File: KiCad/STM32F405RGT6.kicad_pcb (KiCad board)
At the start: 4 copper layers, 101.6 x 101.6 mm, 61 parts, among them J1 Conn_02x05_Odd_Even, J2 USB_C_Receptacle_USB2.0, J3 Conn_02x32_Odd_Even, J4 Conn_02x20_Odd_Even, SW1 TS-1187A, SW2 TS-1187A, U1 M24C02-RMN, U2 STM32F405RGTx, U3 AMS1117-3.3, U4 SRV05-4, Y1 16MHz

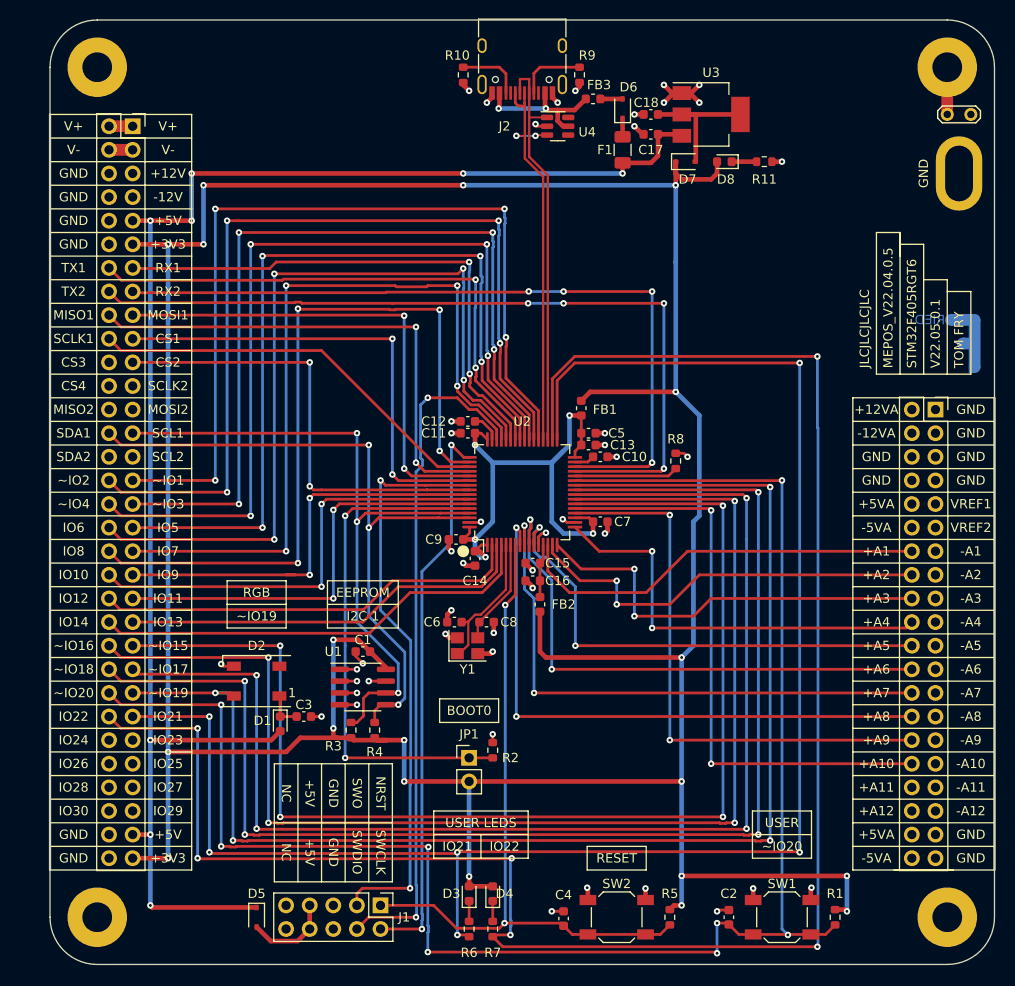
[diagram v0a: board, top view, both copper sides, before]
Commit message: Fixed some DRC errors
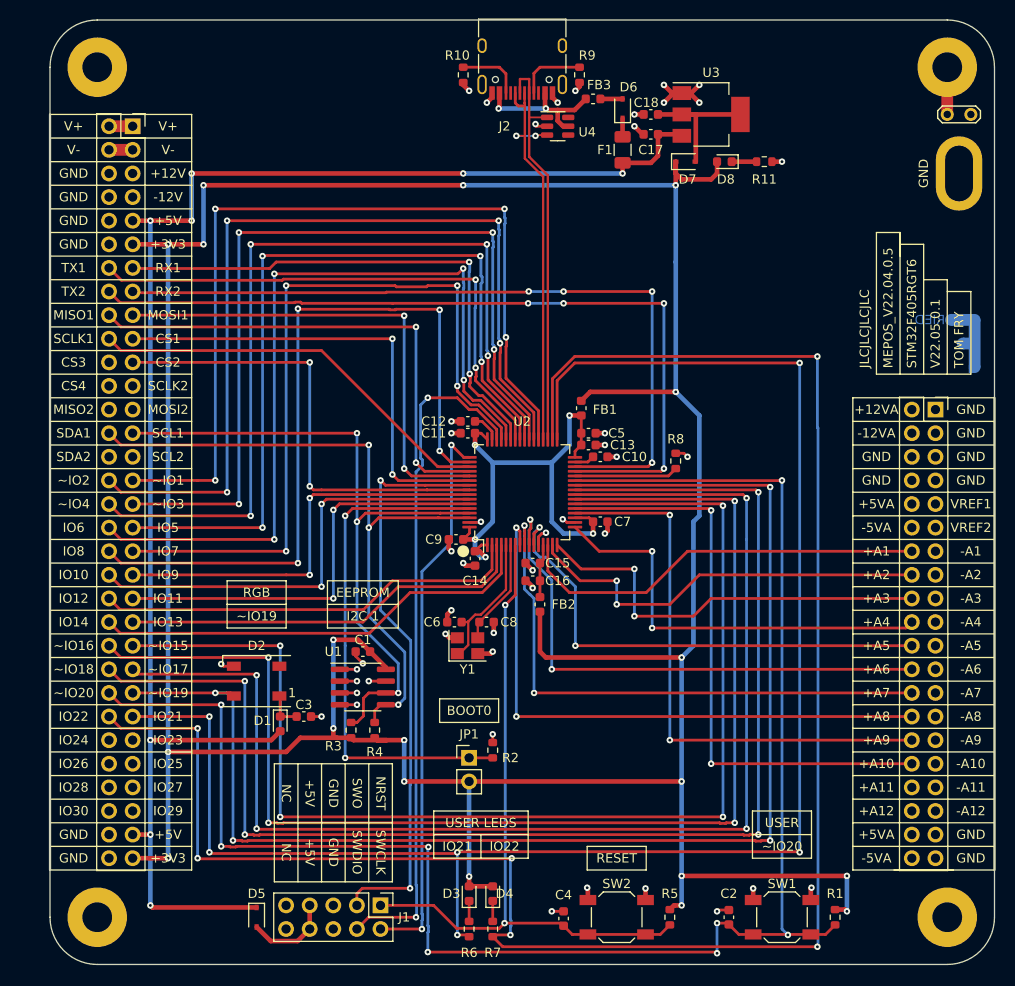
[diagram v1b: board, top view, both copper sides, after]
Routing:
- net /VDD_Decoupling: track 57.9 -> 56.1 mm
- net GPIO9: track 45.6 -> 44.6 mm
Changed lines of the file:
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@@
   (segment (start 89.526882 95.068119) (end 89.523186 95.068119) (width 0.5) (layer "F.Cu") (net 1))
   (segment (start 68.785 105.08) (end 70.625 105.08) (width 0.3) (layer "F.Cu") (net 1))
-  (segment (start 113.17 127.305) (end 113.245 127.38) (width 0.3) (layer "F.Cu") (net 1))
   (segment (start 91.655 41.815) (end 91.655 42.29) (width 0.5) (layer "F.Cu") (net 1))
   (segment (start 90.945 89.135555) (end 90.958029 89.122526) (width 0.3) (layer "F.Cu") (net 1))
@@
   (segment (start 105.575 41.82) (end 106.58 41.82) (width 0.5) (layer "F.Cu") (net 1))
   (segment (start 90.155 90.435) (end 90.155 89.559639) (width 0.3) (layer "F.Cu") (net 1))
-  (segment (start 101.74 127.305) (end 101.665 127.38) (width 0.3) (layer "F.Cu") (net 1))
   (segment (start 85.015 102.12) (end 85.23 101.905) (width 0.5) (layer "F.Cu") (net 1))
   (segment (start 113.245 128.63) (end 113.245 127.38) (width 0.5) (layer "F.Cu") (net 1))
@@
   (segment (start 63.005 93.65) (end 46.495 93.65) (width 0.3) (layer "F.Cu") (net 25))
   (segment (start 65.93 85.01) (end 82.73 85.01) (width 0.3) (layer "F.Cu") (net 25))
-  (segment (start 63.994259 93.65) (end 63.005 93.65) (width 0.3) (layer "F.Cu") (net 25))
   (segment (start 65.545 85.395) (end 65.93 85.01) (width 0.3) (layer "F.Cu") (net 25))
   (via (at 65.545 93.65) (size 0.7) (drill 0.3) (layers "F.Cu" "B.Cu") (net 25))
@@
   (segment (start 83.953802 97.93048) (end 86.655 95.229282) (width 0.25) (layer "F.Cu") (net 91))
   (segment locked (start 134.125 44.12) (end 134.125 39.04) (width 1.27) (layer "F.Cu") (net 92))
-  (segment locked (start 134.379 39.294) (end 134.125 39.04) (width 1.27) (layer "F.Cu") (net 92))
   (segment (start 82.69 113.335) (end 85.23 113.335) (width 0.3) (layer "F.Cu") (net 95))
   (segment (start 81.028564 86.50952) (end 81.029044 86.51) (width 0.3) (layer "F.Cu") (net 95))
@@
   (segment (start 89.19 44.44) (end 89.155 44.405) (width 0.2) (layer "F.Cu") (net 104))
   (segment (start 91.155 50.68) (end 91.155 79.085) (width 0.254) (layer "F.Cu") (net 104))
-  (segment (start 89.154511 41.814511) (end 89.155 41.815) (width 0.3) (layer "F.Cu") (net 104))
   (segment (start 89.155 41.815) (end 89.155 48.68) (width 0.254) (layer "F.Cu") (net 104))
   (segment (start 89.155 48.68) (end 91.155 50.68) (width 0.254) (layer "F.Cu") (net 104))
@@
   (segment (start 85.23 81.585) (end 91.58 81.585) (width 0.5) (layer "B.Cu") (net 105))
   (segment (start 84.4555 91.745) (end 83.96 91.745) (width 0.5) (layer "B.Cu") (net 105))
-  (segment (start 91.58 81.585) (end 92.85 80.315) (width 0.5) (layer "B.Cu") (net 105))
   (segment (start 85.23 87.935) (end 85.23 81.585) (width 0.5) (layer "B.Cu") (net 105))
   (segment (start 91.58 87.935) (end 91.58 81.585) (width 0.5) (layer "B.Cu") (net 105))

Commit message: Updated PCB
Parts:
- moved U4 3.30 mm to (88.9, 45.4)
- moved JP1 1.27 mm to (82.7, 112.1)
- moved R2 1.08 mm to (85.2, 111.4)
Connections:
- U4 pad 1: /STM32_USBD- -> /STM32_USBD+
- U4 pad 3: /STM32_USBD+ -> unconnected-(U4-Pad3)
- U4 pad 6: unconnected-(U4-Pad6) -> /STM32_USBD-
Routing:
- net GPIO7: track 82.6 -> 63.3 mm, vias 4 -> 2
- net GPIO8: track 82.4 -> 66.1 mm
- net GPIO15~: track 131.4 -> 123.4 mm
- net GPIO16~: track 137.6 -> 130.9 mm
- net GPIO17~: track 137.0 -> 131.8 mm
- net GND: track 64.5 -> 69.6 mm, vias 45 -> 47
- net GPIO21: track 182.6 -> 177.6 mm
- net SCLK1: track 44.5 -> 48.9 mm, vias 0 -> 2
- net GPIO20~: track 181.1 -> 176.6 mm
- net GPIO18~: track 143.7 -> 139.7 mm
- net GPIO19~: track 145.4 -> 141.8 mm
- net GPIO22: track 203.2 -> 199.7 mm
- net /STM32_USBD+: track 44.6 -> 41.2 mm, vias 2 -> 0
- net SWDIO: track 73.4 -> 70.3 mm
- net CS2: track 49.7 -> 46.8 mm
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
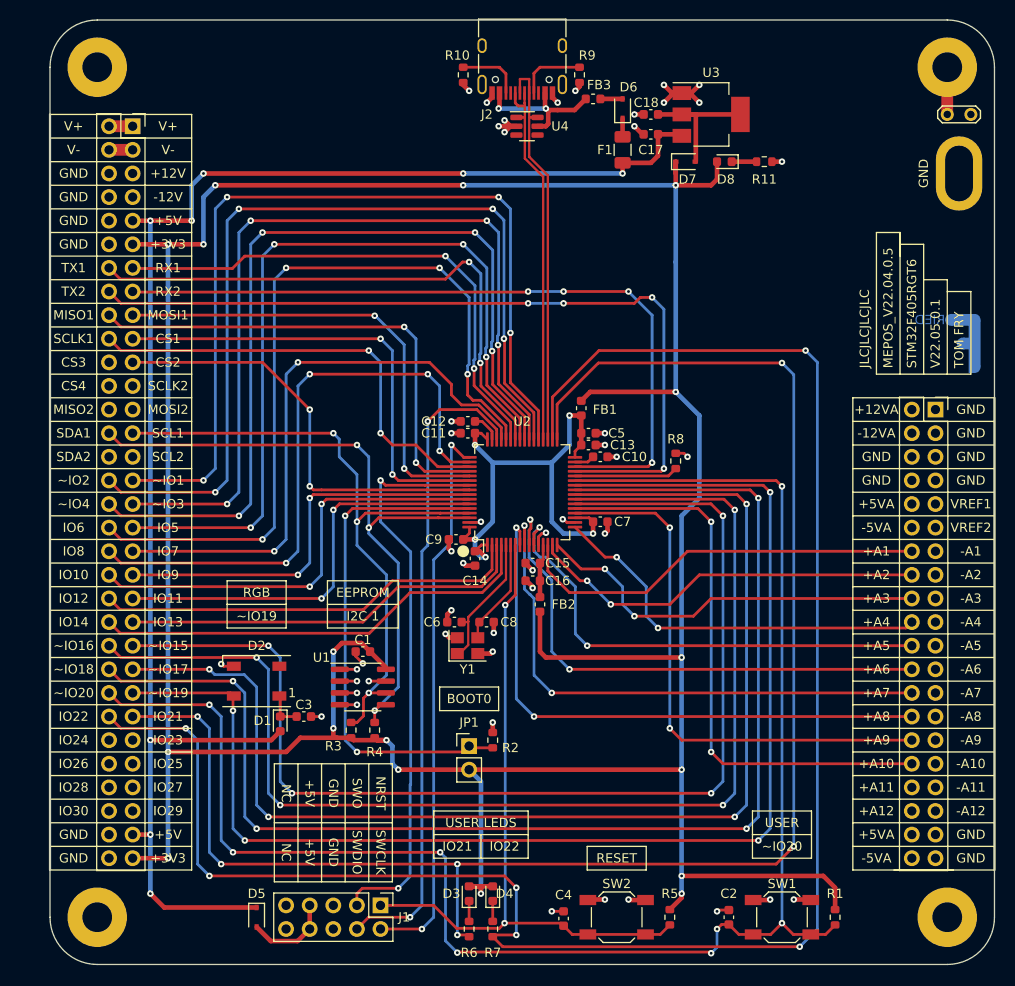
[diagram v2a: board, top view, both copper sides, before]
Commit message: Changed Pin Mapping
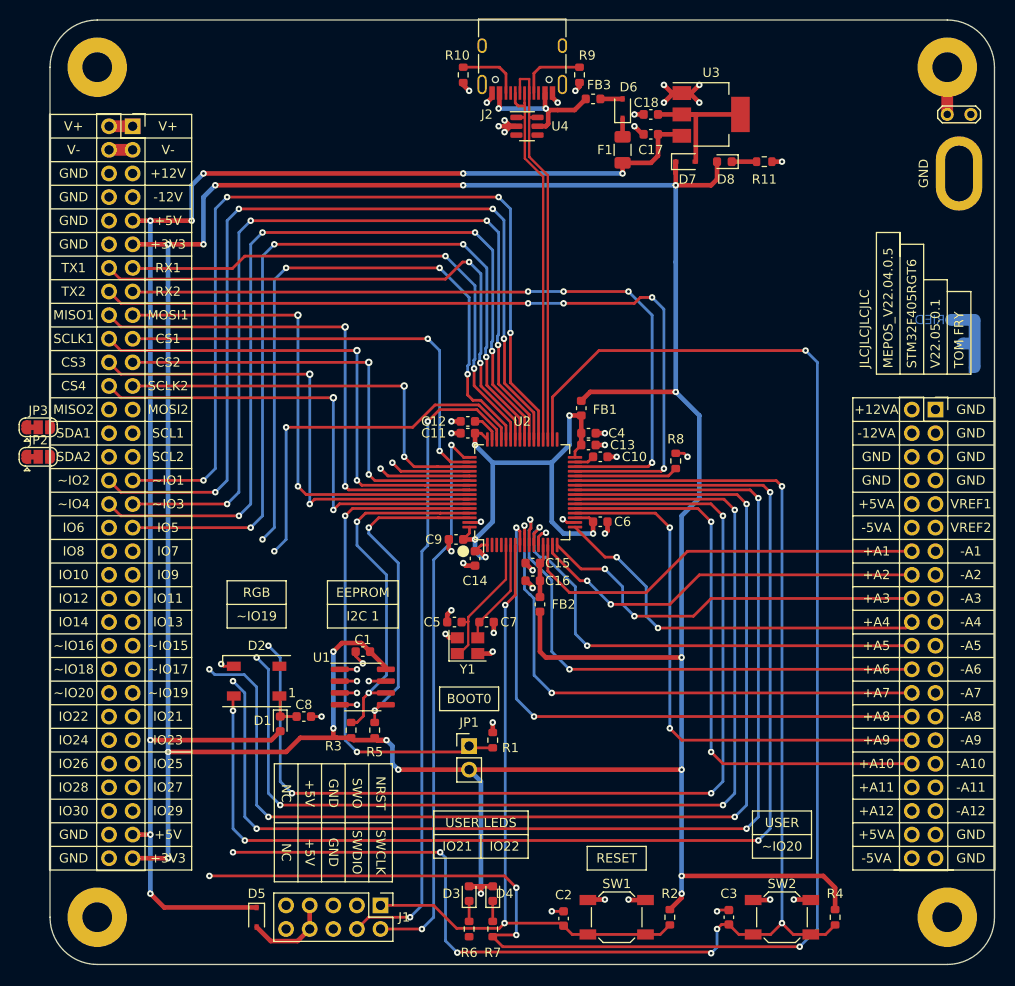
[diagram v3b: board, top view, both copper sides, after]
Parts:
- added JP2: SDA_Jumper, Jumper:SolderJumper-3_P1.3mm_Bridged12_RoundedPad1.0x1.5mm, F.Cu at (36.3, 81.0)
- added JP3: SDA_Jumper, Jumper:SolderJumper-3_P1.3mm_Bridged12_RoundedPad1.0x1.5mm, F.Cu at (36.3, 77.8)
- renumbered C4 to C2, C2 to C3, C5 to C4, C6 to C5, C7 to C6, C8 to C7, C3 to C8, JP2 to JP4, R2 to R1, R5 to R2, R1 to R4, R4 to R5, SW2 to SW1, SW1 to SW2
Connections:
- C3 pad 1: GPIO20~ -> GPIO16~
- D2 pad 4: GPIO19~ -> GPIO15~
- J1 pad 3: SWO -> unconnected-(J1-Pad3)
- R4 pad 2: GPIO20~ -> GPIO16~
- R6 pad 2: GPIO21 -> GPIO17~
- R7 pad 2: GPIO22 -> GPIO18~
- SW2 pad 2: GPIO20~ -> GPIO16~
- U2 pad 2: GPIO12 -> GPIO8
- U2 pad 22: GPIO15~ -> GPIO11
- U2 pad 23: GPIO16~ -> GPIO12
- U2 pad 24: GPIO17~ -> GPIO13
- U2 pad 25: GPIO18~ -> GPIO14
- U2 pad 26: GPIO19~ -> GPIO15~
- U2 pad 27: GPIO20~ -> GPIO16~
- U2 pad 3: GPIO13 -> GPIO9
- U2 pad 33: GPIO21 -> GPIO17~
- U2 pad 34: GPIO22 -> GPIO18~
- U2 pad 4: GPIO14 -> GPIO10
- U2 pad 50: GPIO8 -> CS1
- U2 pad 51: SCLK1 -> SCLK2
- U2 pad 52: MISO1 -> MISO2
- U2 pad 53: MOSI1 -> MOSI2
- U2 pad 54: CS1 -> CS2
- U2 pad 55: SWO -> SCLK1
- U2 pad 56: CS2 -> MISO1
- U2 pad 57: GPIO9 -> MOSI1
- U2 pad 58: GPIO10 -> CS3
- U2 pad 59: GPIO11 -> CS4
- U2 pad 61: SCL1 -> Net-(JP2-Pad2)
- U2 pad 62: SDA1 -> Net-(JP3-Pad2)
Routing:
- net GPIO22: track 199.7 -> 0.00 mm, vias 6 -> 0
- net GPIO21: track 177.6 -> 0.00 mm, vias 6 -> 0
- net GPIO20~: track 176.6 -> 0.00 mm, vias 8 -> 0
- net GPIO19~: track 141.8 -> 0.00 mm, vias 4 -> 0
- net GPIO17~: track 131.8 -> 0.00 mm, vias 4 -> 0
- net GPIO13: track 44.3 -> 123.6 mm, vias 0 -> 4
- net GPIO14: track 48.4 -> 125.8 mm, vias 0 -> 4
- net GPIO12: track 46.1 -> 114.5 mm, vias 0 -> 4
- net GPIO8: track 66.1 -> 0.00 mm, vias 4 -> 0
- net GPIO11: track 45.3 -> 108.8 mm, vias 2 -> 4
- net SWO: track 61.5 -> 0.00 mm, vias 2 -> 0
- net CS3: track 0.00 -> 53.5 mm, vias 0 -> 2
- net CS4: track 0.00 -> 51.6 mm, vias 0 -> 2
- net GPIO10: track 47.7 -> 0.00 mm, vias 2 -> 0
- net SCLK2: track 0.00 -> 44.3 mm, vias 0 -> 2
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
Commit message: Updated PCB and Schematic
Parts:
- JP2: value SDA_Jumper -> SCL_Jumper; footprint Jumper:SolderJumper-3_P1.3mm_Bridged12_RoundedPad1.0x1.5mm -> Jumper:SolderJumper-2_P1.3mm_Open_RoundedPad1.0x1.5mm
- JP3: footprint Jumper:SolderJumper-3_P1.3mm_Bridged12_RoundedPad1.0x1.5mm -> Jumper:SolderJumper-2_P1.3mm_Open_RoundedPad1.0x1.5mm
- moved JP2 21.7 mm to (57.9, 79.0), turned to -90 degrees
- moved JP3 18.8 mm to (54.8, 81.6), turned to -90 degrees
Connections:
- JP2 pad 2: Net-(JP2-Pad2) -> SCL2
- JP3 pad 2: Net-(JP3-Pad2) -> SDA2
- U2 pad 61: Net-(JP2-Pad2) -> SCL1
- U2 pad 62: Net-(JP3-Pad2) -> SDA1
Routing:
- net GPIO17~: track 0.00 -> 198.4 mm, vias 0 -> 6
- net GPIO10: track 0.00 -> 46.1 mm
- net GPIO8: track 0.00 -> 45.1 mm
- net GPIO9: track 0.00 -> 42.5 mm
- net SDA1: track 36.1 -> 73.3 mm
- net MISO2: track 8.68 -> 44.1 mm, vias 1 -> 2
- net GPIO16~: track 148.4 -> 183.2 mm, vias 7 -> 8
- net MOSI2: track 9.89 -> 42.9 mm, vias 1 -> 2
- net GPIO18~: track 174.0 -> 206.3 mm, vias 5 -> 6
- net SCL1: track 39.2 -> 70.7 mm, vias 2 -> 4
- net GPIO12: track 114.5 -> 136.0 mm
- net GPIO11: track 108.8 -> 128.5 mm
- net GPIO14: track 125.8 -> 144.8 mm
- net GPIO6: track 68.8 -> 85.8 mm
- net GPIO15~: track 130.8 -> 147.4 mm, vias 4 -> 5
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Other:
- board text added: "I2C Selectors"

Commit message: Changed some components
added a PNP mosfet onto the onboard 3.3V regulator to stop the diode drop.
changed the ESD protection on the USB to allow for more clearance
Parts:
- removed the D7 at (106.0, 49.2)
- removed U4: SRV05-4, Package_TO_SOT_SMD:SOT-23-6
- added D10: PSM712-LF-T7, Package_TO_SOT_SMD:SOT-23, F.Cu at (90.9, 46.2)
- added D2: 1N5819WS, Diode_SMD:D_SOD-323, F.Cu at (106.6, 49.5)
- added D9: PSM712-LF-T7, Package_TO_SOT_SMD:SOT-23, F.Cu at (86.9, 46.2)
- added Q1: AO3401A, Package_TO_SOT_SMD:SOT-23, F.Cu at (111.3, 50.4)
- moved R8 6.76 mm to (115.1, 42.5), turned to 90 degrees
- moved D6 5.73 mm to (115.1, 46.3), turned to -90 degrees
- moved C3 0.25 mm to (110.6, 130.7)
- moved D7 0.25 mm to (59.8, 130.7)
- moved H2 0.25 mm to (42.7, 130.7)
- moved H3 0.25 mm to (134.1, 130.7)
- moved R2 0.25 mm to (104.3, 130.7)
- moved R4 0.25 mm to (122.1, 130.7)
- moved SW1 0.25 mm to (98.6, 130.7)
- moved SW2 0.25 mm to (116.3, 130.7)
- moved C1 0.25 mm to (71.3, 102.2)
- moved C12 0.25 mm to (82.5, 78.7)
- moved C13 0.25 mm to (82.5, 77.4)
- moved C15 0.25 mm to (102.2, 44.4)
- moved C17 0.25 mm to (89.5, 92.6)
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- renumbered C9 to C10, C10 to C11, C11 to C12, C12 to C13, C13 to C14, C18 to C15, C14 to C16, C15 to C17, C16 to C18, C17 to C9, D2 to D3, D3 to D4, D4 to D5, D8 to D6, D5 to D7, D6 to D8, R9 to R10, R10 to R11, R11 to R8, R8 to R9, U3 to U2, U2 to U3
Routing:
- net +3V3: track 369.1 -> 372.6 mm
- net +5V: track 168.0 -> 170.7 mm
- net /USB_5V: track 16.4 -> 14.8 mm
- net /ONBOARD_+3V3: track 15.5 -> 16.8 mm
- net GND: track 69.1 -> 70.3 mm, vias 47 -> 49
- net SCL1: track 70.7 -> 69.5 mm
- net GPIO7: track 55.2 -> 54.1 mm
- net MISO1: track 56.6 -> 55.9 mm
- net MOSI1: track 55.0 -> 54.3 mm
- net CS3: track 51.9 -> 51.2 mm
- net CS2: track 48.6 -> 47.8 mm
- net SCLK2: track 44.3 -> 43.6 mm
- net MISO2: track 44.1 -> 43.5 mm
- net /STM32_USBD+: track 41.2 -> 41.8 mm
- net /STM32_USBD-: track 42.9 -> 43.5 mm

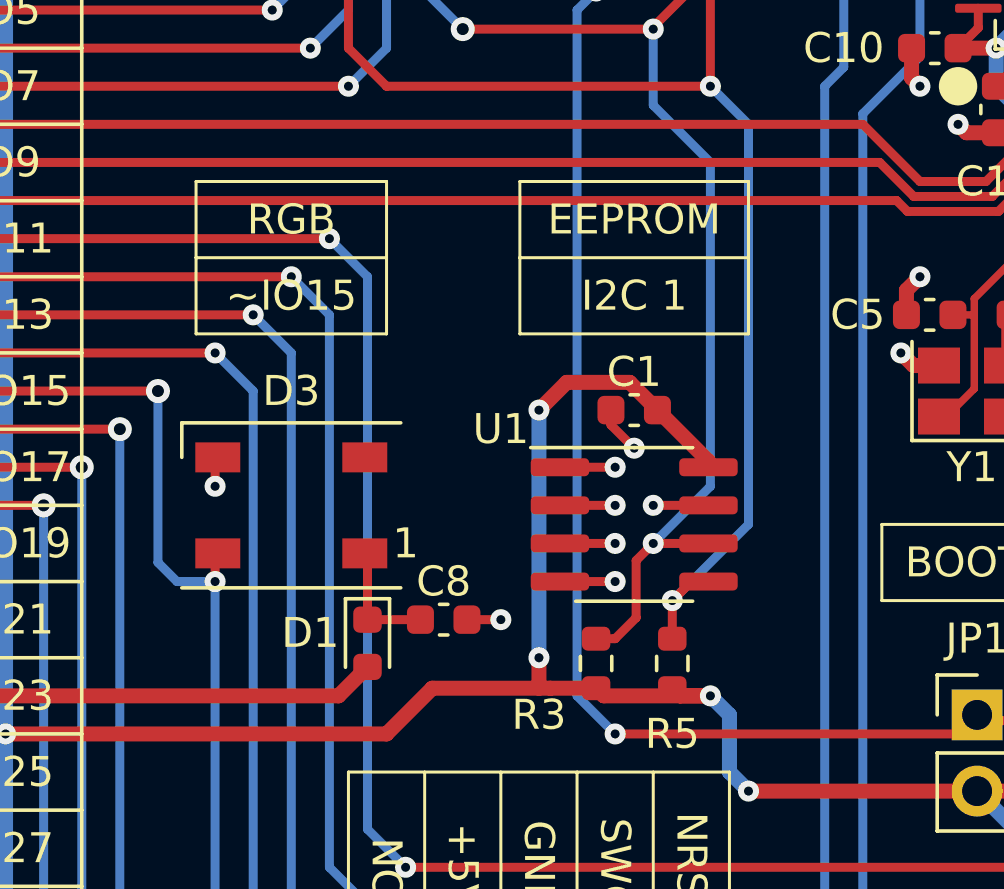
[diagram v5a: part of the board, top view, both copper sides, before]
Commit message: Added Datasheets
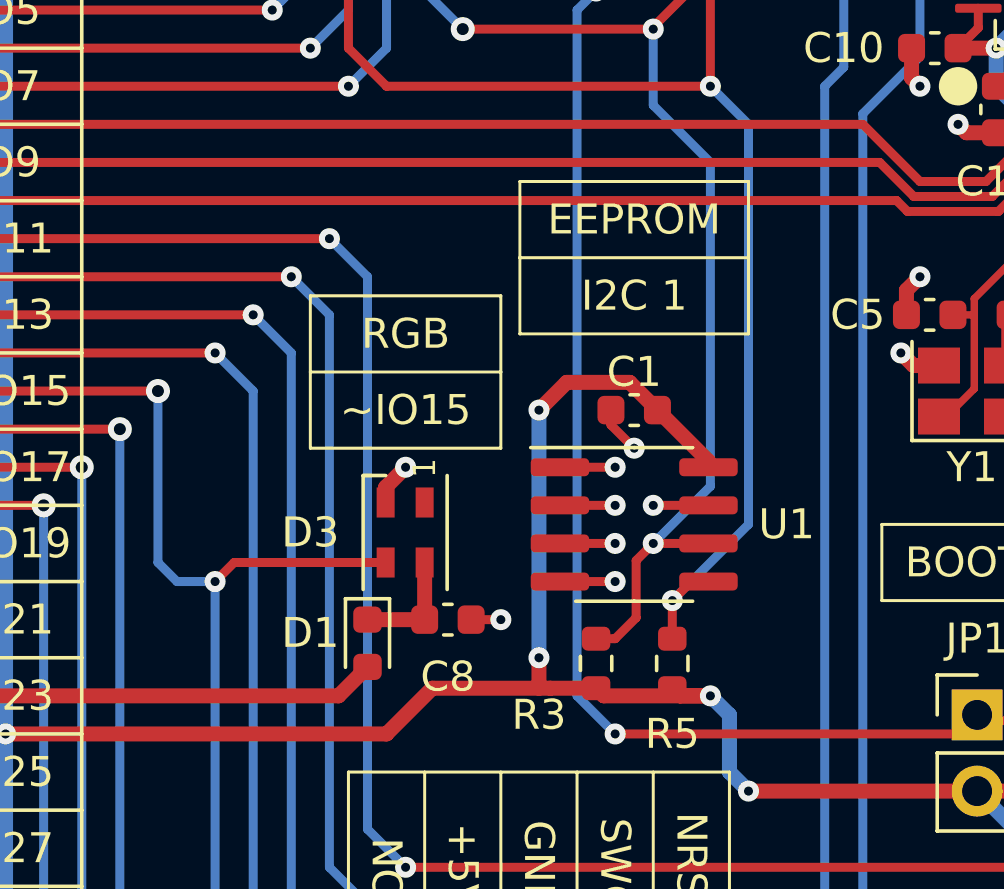
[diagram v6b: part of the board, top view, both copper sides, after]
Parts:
- D3: value WS2812B -> SK6805; footprint LED_SMD:LED_WS2812B_PLCC4_5.0x5.0mm_P3.2mm -> LED_SMD:LED_SK6805_PLCC4_2.4x2.7mm_P1.3mm
- J2: value USB_C_Receptacle_USB2.0 -> USB_C_2.0
- moved D3 3.90 mm to (63.6, 106.2), turned to -90 degrees
- moved C8 0.14 mm to (65.0, 109.1)
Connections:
- D3 pad 1: /LED_Decoupling -> unconnected-(D3-Pad1)
- D3 pad 2: unconnected-(D3-Pad2) -> GND
- D3 pad 3: GND -> GPIO15~
- D3 pad 4: GPIO15~ -> /LED_Decoupling
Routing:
- net GPIO15~: track 147.4 -> 152.4 mm
